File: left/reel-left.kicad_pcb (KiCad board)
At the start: 2 copper layers, 144.5 x 95 mm, 53 parts, among them J1 Conn_01x02, SW1 SW_Push, SW10 SW_Push, SW11 SW_Push, SW12 SW_Push, SW13 SW_Push, SW14 SW_Push, SW15 SW_Push, SW16 SW_Push, SW17 SW_Push, SW18 SW_Push, SW19 SW_Push, SW2 SW_Push, SW20 SW_Push, SW21 SW_Push, SW22 SW_Push, SW24 SW_SPDT, SW25 RotaryEncoder, SW3 SW_Push, SW4 SW_Push, SW5 SW_Push, SW6 SW_Push, SW7 SW_Push, SW8 SW_Push, SW9 SW_Push

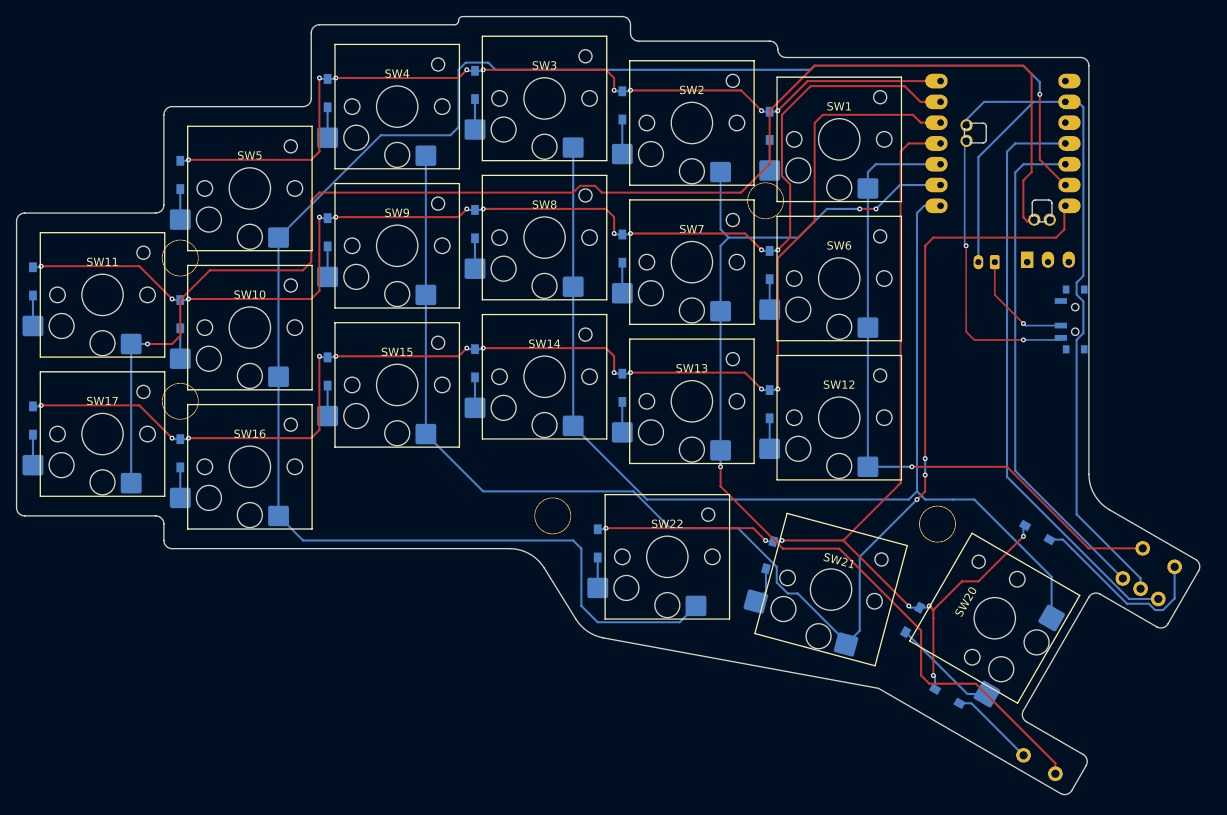
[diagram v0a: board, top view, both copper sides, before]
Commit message: Update ReeL switch footprints and board layouts
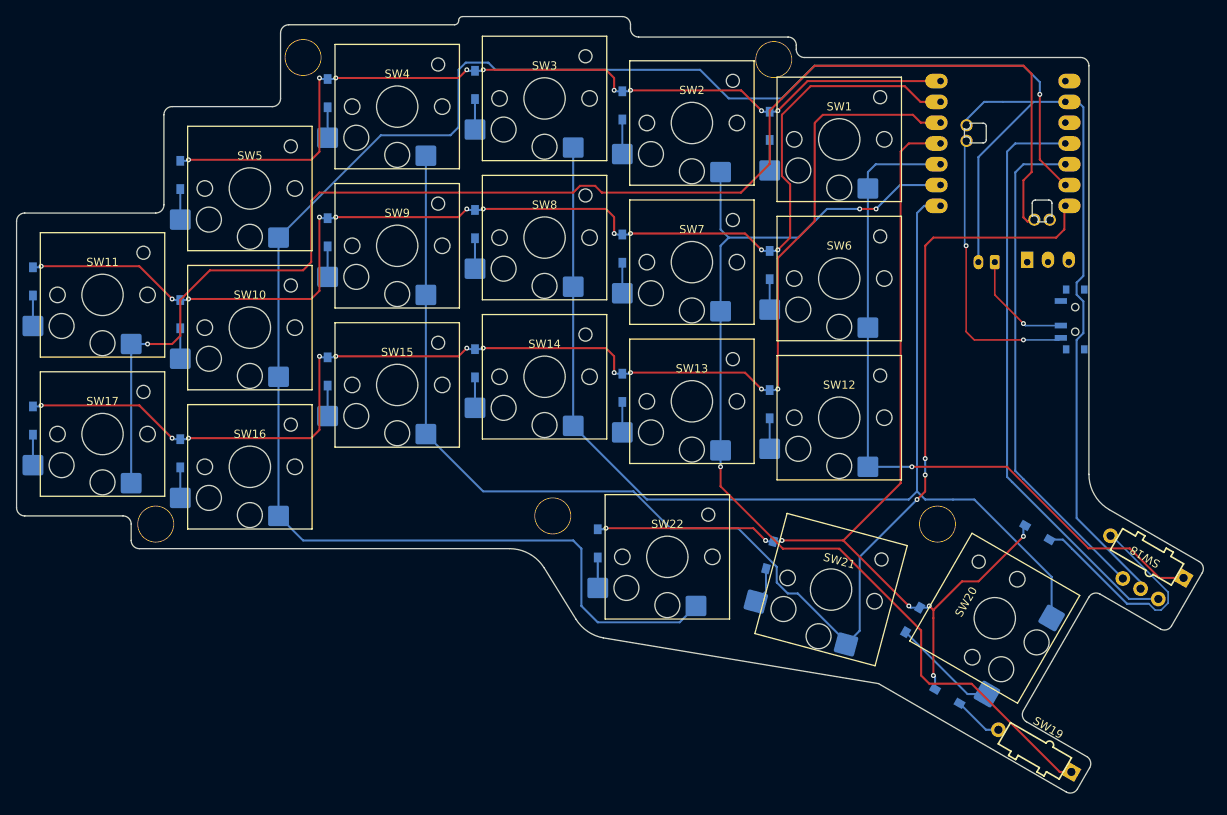
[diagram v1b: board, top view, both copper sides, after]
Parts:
- SW18: footprint reel:SideTactSwitch_2pin -> reel:Switch_E-Switch_TS2_Vertical_THT
- SW19: footprint reel:SideTactSwitch_2pin -> reel:Switch_E-Switch_TS2_Vertical_THT_Mirrored
- moved Ref** 28.7 mm to (112.0, 58.0)
- moved Ref** 17.3 mm to (169.5, 58.2)
- moved Ref** 15.3 mm to (94.0, 115.0)
- moved SW19 1.77 mm to (201.4, 142.7), turned to -30 degrees
- moved SW18 1.43 mm to (215.1, 119.0), turned to 150 degrees
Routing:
- net Col0: track 83.0 -> 89.5 mm
- net Net-(D18-A): track 23.5 -> 29.5 mm
- net Net-(D19-A): track 10.4 -> 6.08 mm
- net Col4: track 216.5 -> 219.4 mm
- net Col1: track 127.2 -> 128.3 mm
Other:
- board size 144.5 x 95 mm -> 145 x 94.9 mm

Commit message: Update left board and rotary encoder fabrication assets
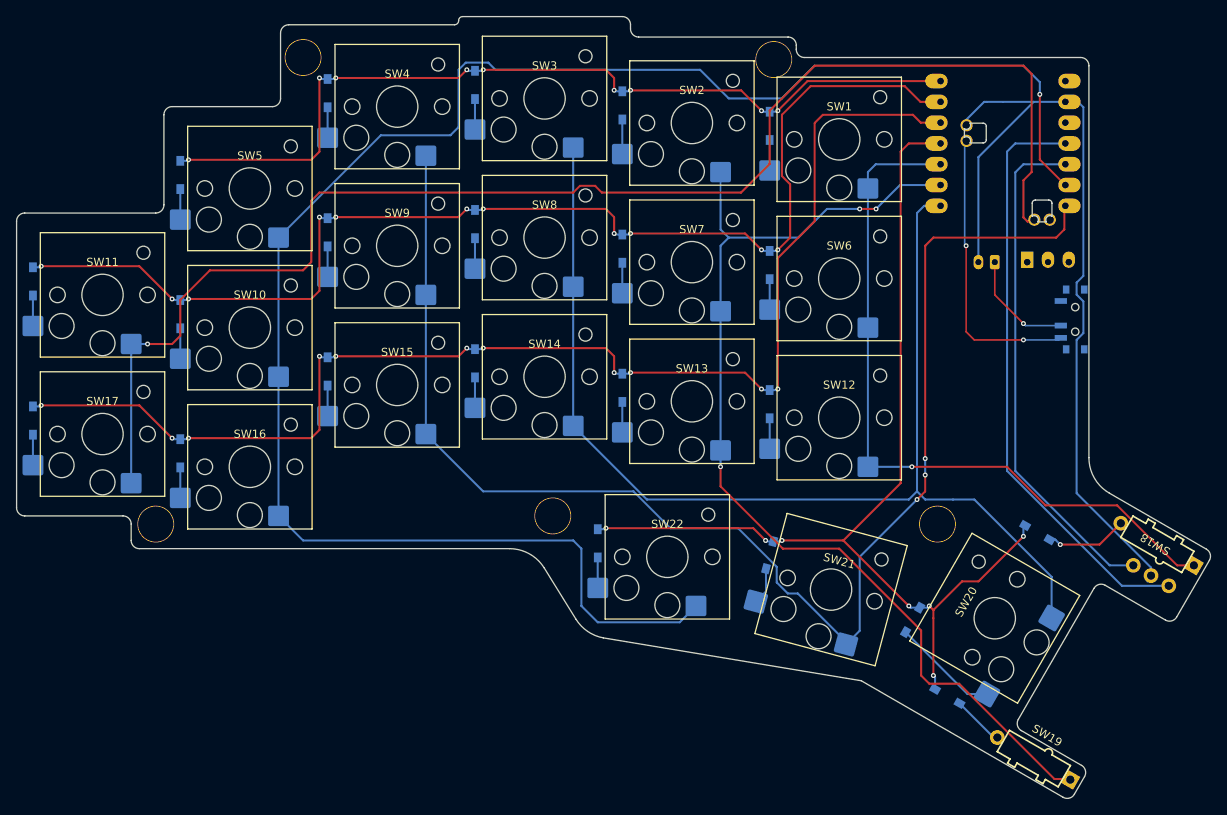
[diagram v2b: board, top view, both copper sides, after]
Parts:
- moved SW25 2.05 mm to (215.6, 121.3)
- moved SW18 1.98 mm to (216.4, 117.5)
- moved SW19 0.95 mm to (201.3, 143.6)
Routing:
- net Net-(D18-A): track 29.5 -> 10.0 mm, vias 0 -> 1
- net Col0: track 89.5 -> 90.1 mm
- net RotA: track 61.8 -> 62.4 mm
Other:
- board size 145 x 94.9 mm -> 145.9 x 95.5 mm
